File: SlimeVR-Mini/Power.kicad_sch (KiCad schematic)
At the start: 3 parts, among them J1 Conn_01x02, U3 TP4056

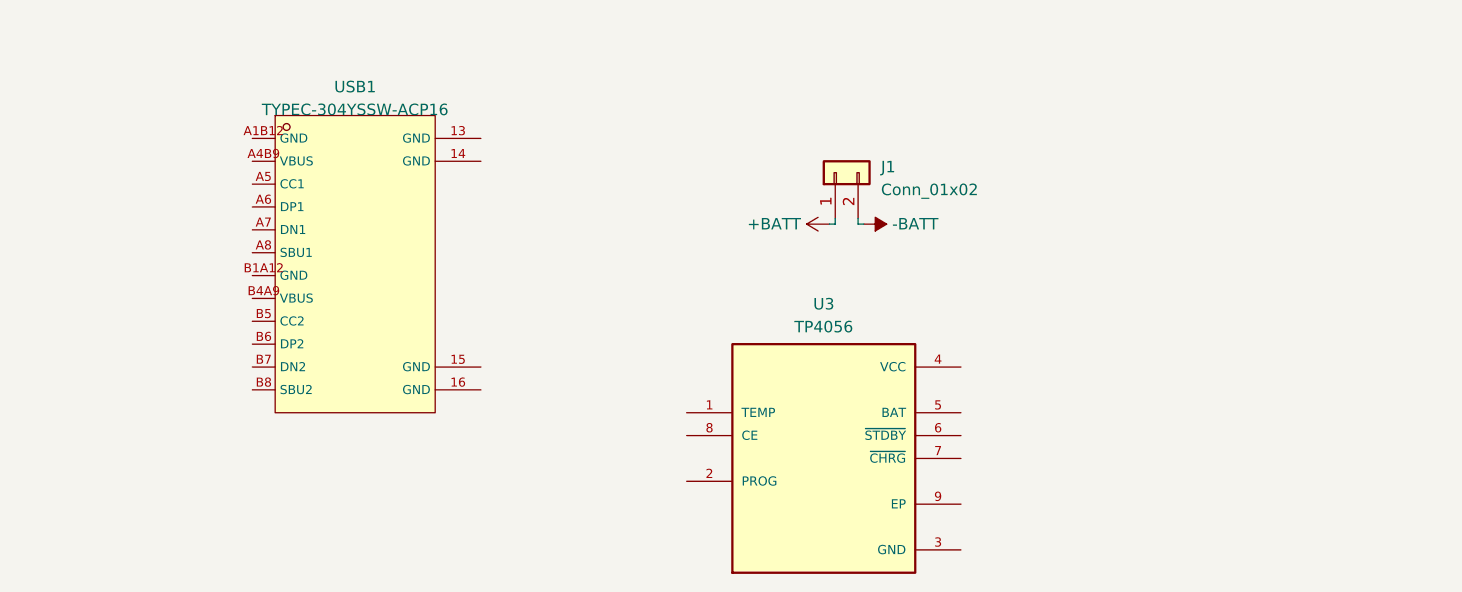
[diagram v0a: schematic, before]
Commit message: added CH340N + schematics development
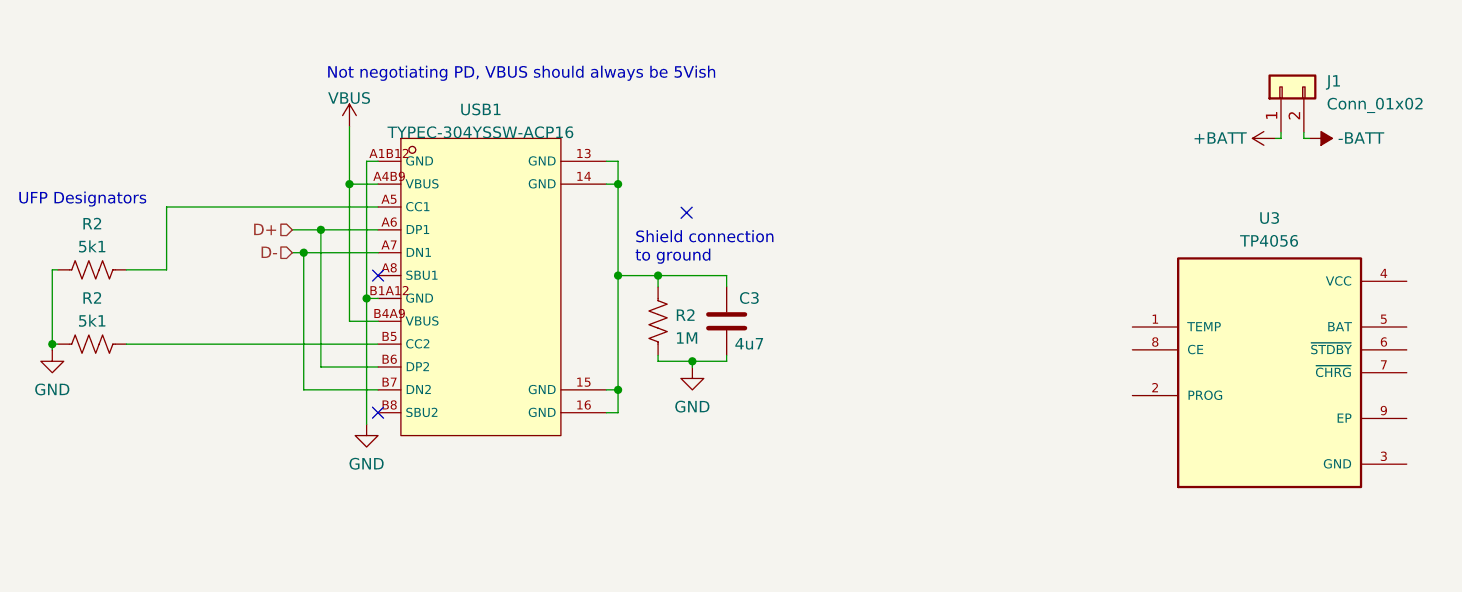
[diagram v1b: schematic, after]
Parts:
- added C3: 4u7, symbol Device:C
- added R2 (x2): 5k1, symbol Device:R_US
- added R2: 1M, symbol Device:R_US
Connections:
- net at USB1.13 (GND): now also USB1.14 (GND), USB1.15 (GND), USB1.16 (GND), C3.1, R2.2
- net GND: now reaches USB1.A1B12 (GND)
- net GND: now also USB1.B1A12 (GND), C3.2, R2.1, R2.1, R2.2
- net VBUS: now reaches USB1.A4B9 (VBUS)
- net VBUS: now also USB1.B4A9 (VBUS)
- net at USB1.A5 (CC1): now also R2.2
- net D+: now reaches USB1.A6 (DP1)
- net D+: now also USB1.B6 (DP2)
- net D-: now reaches USB1.A7 (DN1)
- net D-: now also USB1.B7 (DN2)
- net at USB1.B5 (CC2): now also R2.1
- no-connect marks 0 -> 3
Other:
- note added: "Not negotiating PD, VBUS should always be 5Vish"
- note added: "Shield connection to ground"
- note added: "UFP Designators"
- moved on the sheet: J1, U3, USB1

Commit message: assigned footprints, finished USB-UART sch
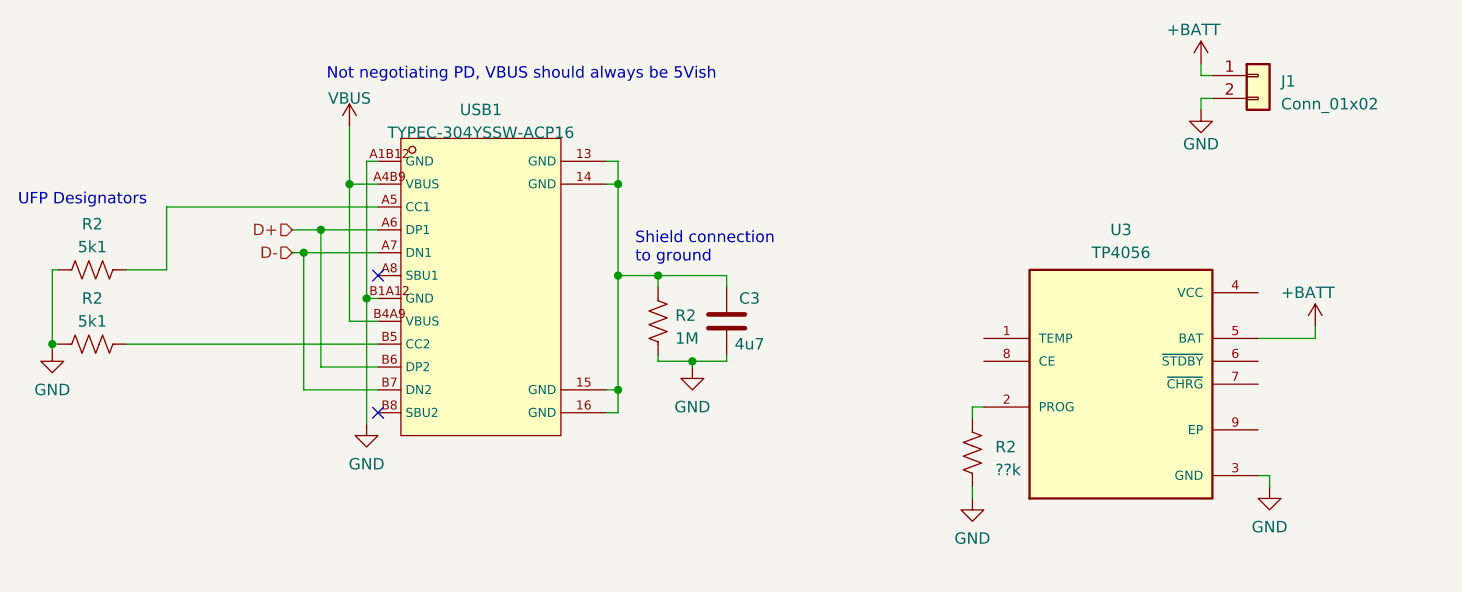
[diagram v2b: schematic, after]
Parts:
- added R2: ??k, Resistor_SMD:R_0402_1005Metric, symbol Device:R_US
- R2: footprint (none) -> Resistor_SMD:R_0402_1005Metric
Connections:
- net -BATT is gone; now on net GND: J1.2 (Pin_2)
- net +BATT: now also U3.5 (BAT)
- net GND: now also U3.3 (GND), R2.1
- net at U3.2 (PROG): now also R2.2
- no-connect marks 3 -> 2
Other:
- moved on the sheet: J1, U3
